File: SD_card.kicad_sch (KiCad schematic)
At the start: 0 parts

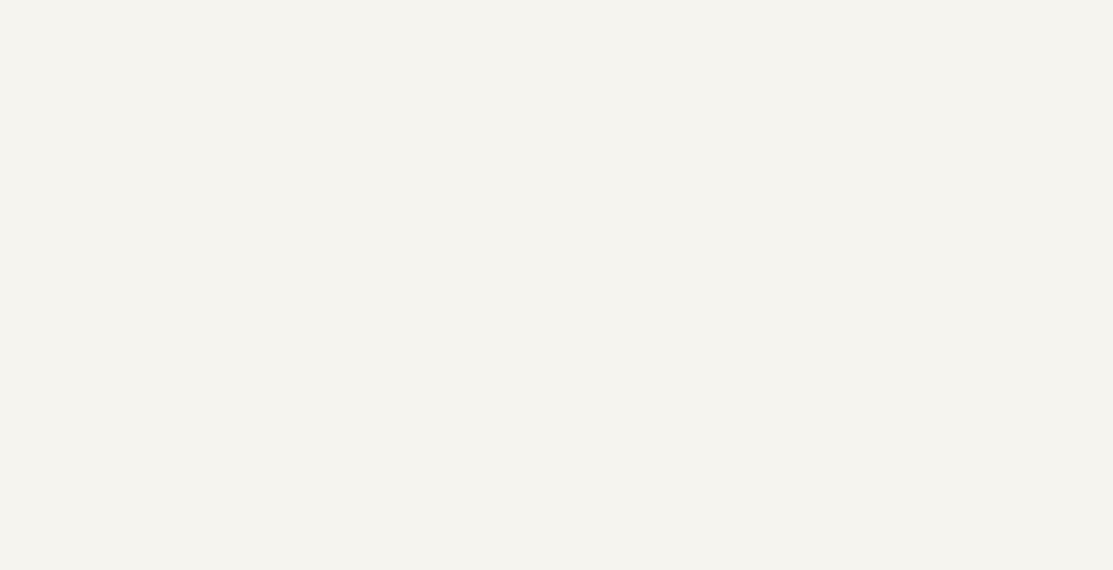
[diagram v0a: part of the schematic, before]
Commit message: Pasted schematics from previous design
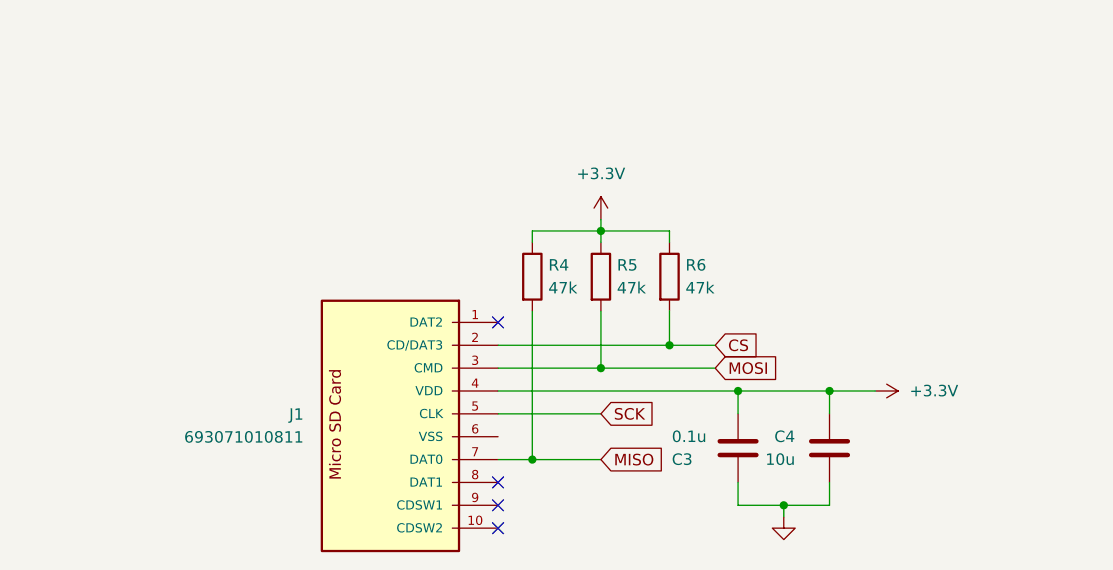
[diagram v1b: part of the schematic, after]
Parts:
- added C3: 0.1u, Capacitor_SMD:C_1206_3216Metric_Pad1.33x1.80mm_HandSolder, symbol Device:C
- added C4: 10u, Capacitor_SMD:C_1206_3216Metric_Pad1.33x1.80mm_HandSolder, symbol Device:C
- added J1: 693071010811, 693071010811:693071010811, symbol 693071010811:693071010811
- added R4, R5, R6: 47k, Resistor_SMD:R_1206_3216Metric_Pad1.30x1.75mm_HandSolder, symbol Device:R
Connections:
- new net: J1.10 (CDSW2), J1.10-1 (CDSW2)
- new net: J1.9 (CDSW1), J1.9-1 (CDSW1)
- new net +3.3V: C3.2, C4.2, J1.4 (VDD), R4.1, R5.1, R6.1
- new net CS: J1.2 (CD/DAT3), R6.2
- new net GND: C3.1, C4.1
- new net MISO: J1.7 (DAT0), R4.2
- new net MOSI: J1.3 (CMD), R5.2
- new net SCK: J1.5 (CLK)
- no-connect marks 0 -> 4

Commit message: Changed a few preferences
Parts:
- C3, C4: footprint Capacitor_SMD:C_1206_3216Metric_Pad1.33x1.80mm_HandSolder -> Capacitor_SMD:C_0603_1608Metric
- R4, R5, R6: footprint Resistor_SMD:R_1206_3216Metric_Pad1.30x1.75mm_HandSolder -> Resistor_SMD:R_0603_1608Metric
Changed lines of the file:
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@@
 			)
 		)
-		(property "Footprint" "Resistor_SMD:R_1206_3216Metric_Pad1.30x1.75mm_HandSolder"
+		(property "Footprint" "Resistor_SMD:R_0603_1608Metric"
 			(at 210.312 124.46 90)
 			(hide yes)
@@
 			)
 		)
-		(property "Footprint" "Capacitor_SMD:C_1206_3216Metric_Pad1.33x1.80mm_HandSolder"
+		(property "Footprint" "Capacitor_SMD:C_0603_1608Metric"
 			(at 246.0752 139.7 0)
 			(hide yes)
@@
 			)
 		)
-		(property "Footprint" "Resistor_SMD:R_1206_3216Metric_Pad1.30x1.75mm_HandSolder"
+		(property "Footprint" "Resistor_SMD:R_0603_1608Metric"
 			(at 225.552 124.46 90)
 			(hide yes)
@@
 			)
 		)
-		(property "Footprint" "Capacitor_SMD:C_1206_3216Metric_Pad1.33x1.80mm_HandSolder"
+		(property "Footprint" "Capacitor_SMD:C_0603_1608Metric"
 			(at 235.9152 139.7 0)
 			(hide yes)
@@
 			)
 		)
-		(property "Footprint" "Resistor_SMD:R_1206_3216Metric_Pad1.30x1.75mm_HandSolder"
+		(property "Footprint" "Resistor_SMD:R_0603_1608Metric"
 			(at 217.932 124.46 90)
 			(hide yes)
